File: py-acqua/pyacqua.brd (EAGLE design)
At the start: 146.4 x 124.4 mm, 35 parts, among them IC1 uln2308, K1 JS-M1-9V-4, K2 JS-M1-9V-4, K3 JS-M1-9V-4, K4 JS-M1-9V-4, T1 BC547, T2 BC547, X1 MSTBA4

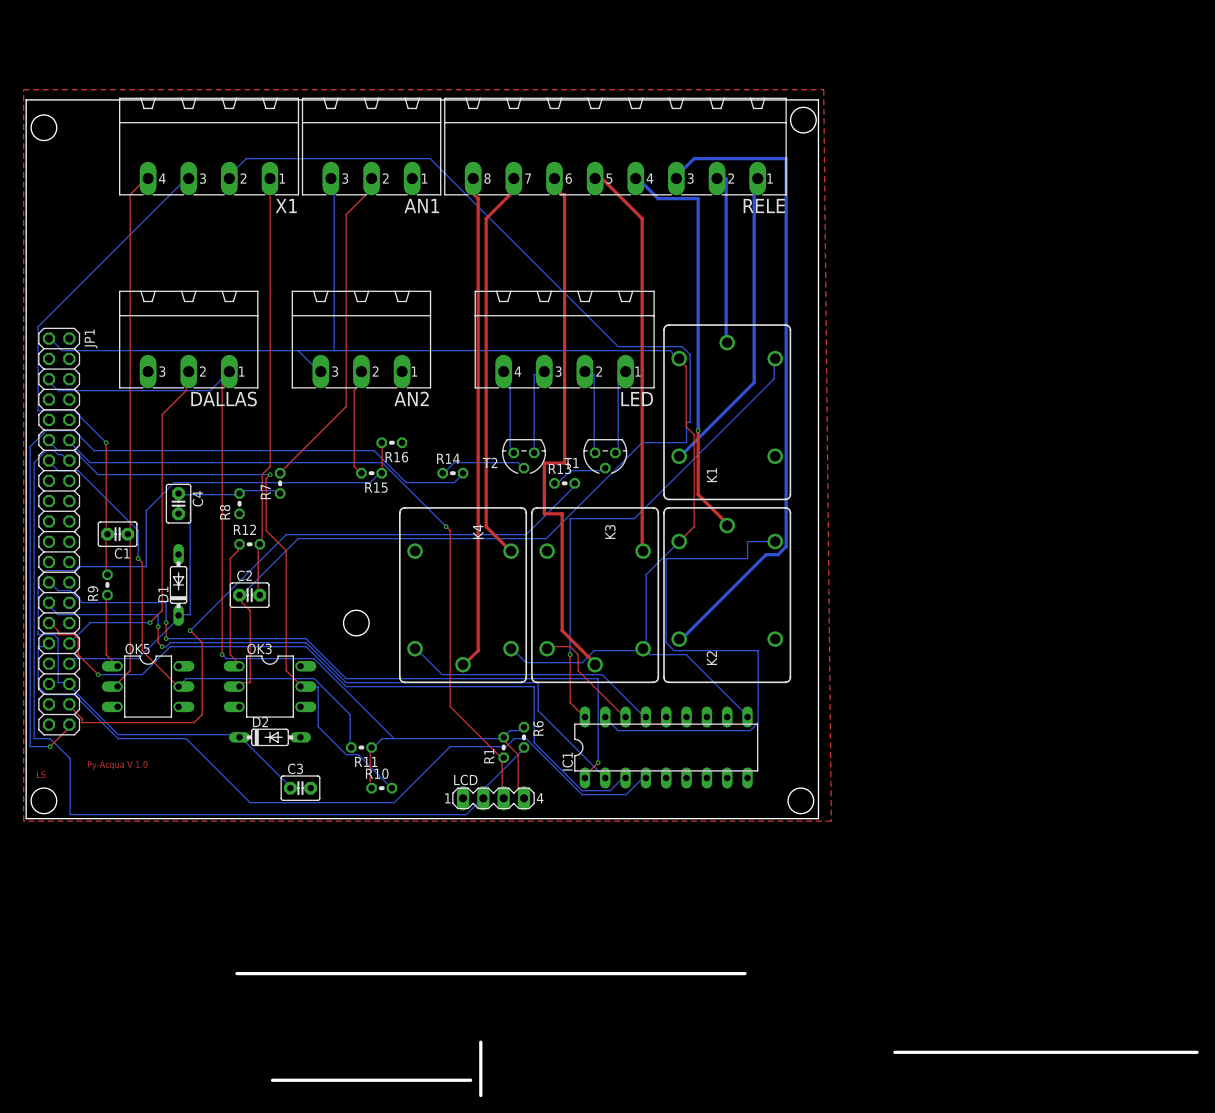
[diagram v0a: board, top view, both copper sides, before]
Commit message: sistemazioni input su py-acqua
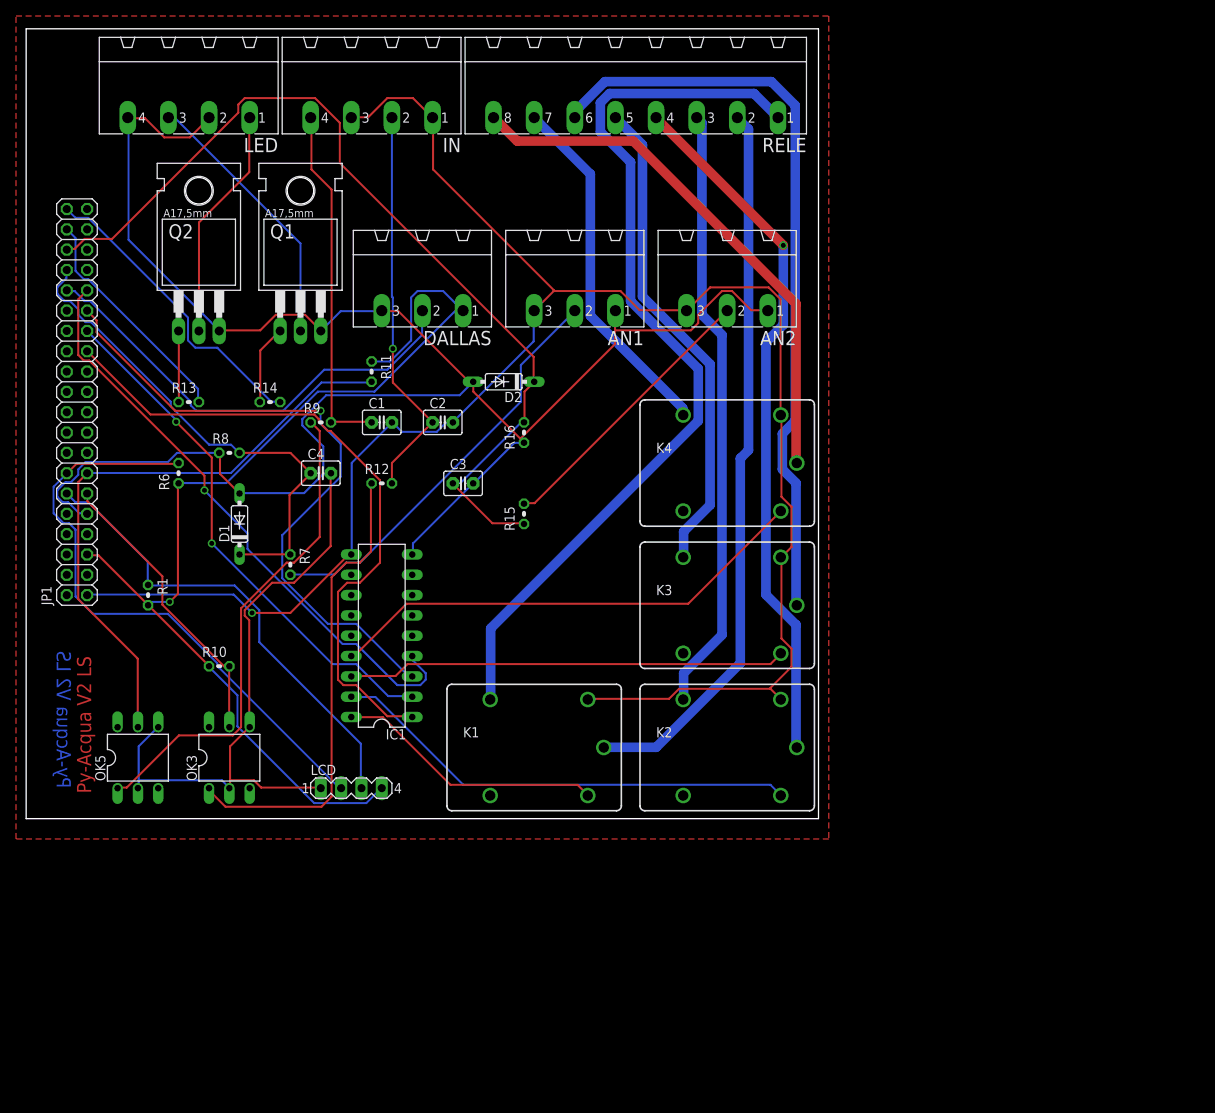
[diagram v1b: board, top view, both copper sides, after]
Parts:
- removed T1, T2: BC547, transistor:TO92
- removed X1: MSTBA4, con-phoenix-508:MSTBA4
- added IN: MSTBA4, con-phoenix-508:MSTBA4
- added Q1, Q2: TIP120, transistor-power:TO220AH
- moved LED 56.7 mm to (20.3, 92.7)
- moved R6 54.4 mm to (19.1, 43.2), turned to 90 degrees
- moved D2 53.2 mm to (59.7, 54.6), turned to 180 degrees
- moved K1 48.4 mm to (63.5, 8.89), turned to 0 degrees
- moved R1 48.4 mm to (15.2, 27.9), turned to 270 degrees
- moved R13 48.1 mm to (20.3, 52.1)
- moved R11 47.0 mm to (43.2, 55.9), turned to 270 degrees
- moved AN2 46.4 mm to (87.6, 68.6)
- moved C3 43.2 mm to (54.6, 41.9)
- moved IC1 38.2 mm to (44.5, 22.9), turned to 90 degrees
- moved K4 36.9 mm to (87.6, 44.5), turned to 0 degrees
- moved C1 35.9 mm to (44.5, 49.5), turned to 0 degrees
- moved R9 33.5 mm to (36.8, 49.5), turned to 0 degrees
- moved C2 32.4 mm to (52.1, 49.5)
- moved AN1 30.3 mm to (68.6, 68.6)
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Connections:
- removed net 3LED: LED.3, T2.3
- removed net 4LED: LED.4, T2.1
- removed net N$2: C2.2, R12.2, X1.1
- removed net N$4: C2.1, OK3.2, X1.2
- removed net N$7: C1.2, R9.2, X1.3
- new net N$5: C2.1, IN.2, R12.2
- net 1LED: now also Q2.C; no longer T1.3
- net 2LED: now also LED.3, Q1.C; no longer LED.2, T1.1
- net 5V: now also C1.2, C2.2, IN.1, IN.3
- net GND: now also LED.2, LED.4, OK3.2, OK5.2, Q1.E, Q2.E
- net N$10: now also IN.4, R9.2; no longer OK5.2, X1.4
- net N$11: now also Q1.B; no longer T2.2
- net N$9: now also Q2.B; no longer T1.2
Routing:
- net GND: track 0.00 -> 313.3 mm
- net N$4: track 157.2 -> 0.00 mm
- net 1: track 39.1 -> 114.4 mm
- net 2: track 21.8 -> 90.6 mm
- net N$7: track 63.9 -> 0.00 mm, vias 1 -> 0
- net PWM3: track 101.9 -> 38.3 mm, vias 1 -> 0
- net PWM2: track 85.3 -> 28.8 mm, vias 1 -> 0
- net 5V: track 180.1 -> 234.0 mm, vias 0 -> 1
- net N$2: track 52.9 -> 0.00 mm
- net N$1: track 9.50 -> 61.8 mm
- net N$5: track 0.00 -> 49.9 mm, vias 0 -> 1
- net N$3: track 16.1 -> 59.2 mm
- net PA24: track 77.5 -> 37.0 mm, vias 1 -> 0
- net O3: track 14.7 -> 54.9 mm
- net SDA0: track 113.4 -> 75.5 mm
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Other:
- board size 146.4 x 124.4 mm -> 99 x 98.7 mm
- board text added: "Py-Acqua V2 LS"
- board text removed: "LS"
- board text removed: "Py-Acqua V 1.0"
